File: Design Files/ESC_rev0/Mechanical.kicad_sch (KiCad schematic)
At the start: 8 parts

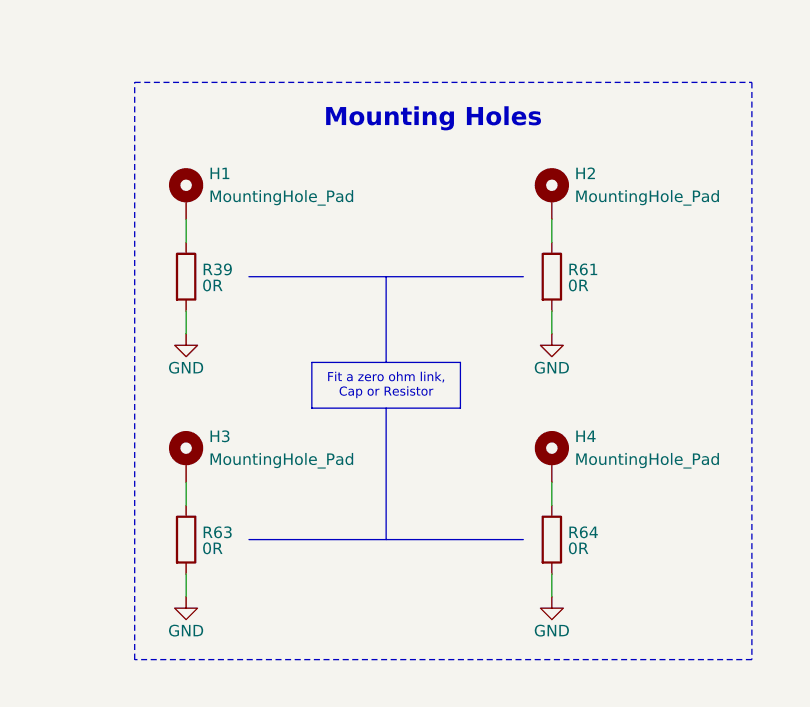
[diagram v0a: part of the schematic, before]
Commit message: UPDATE 12
started schematics revision: edit and added info and circuits to some pages and assigned some footprints for components
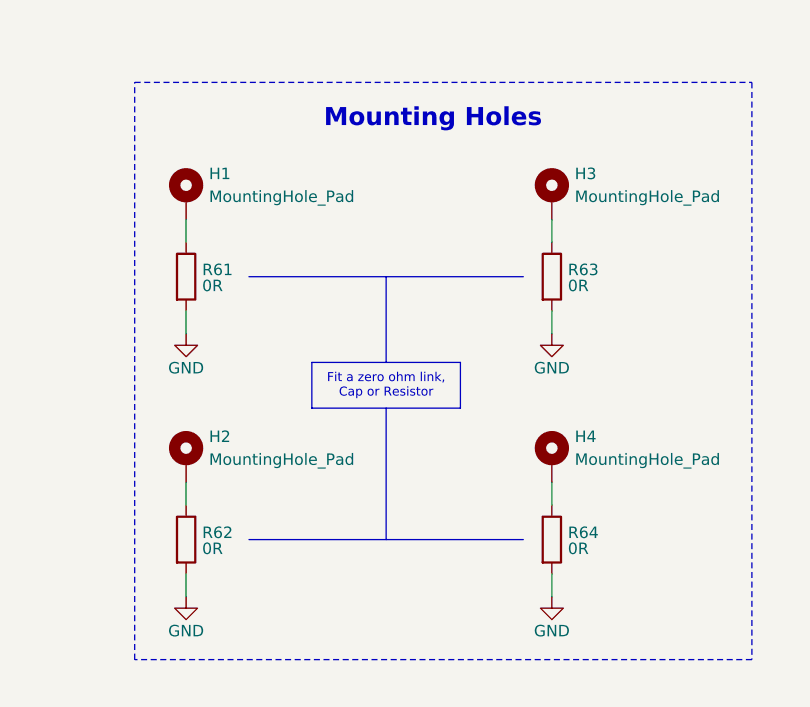
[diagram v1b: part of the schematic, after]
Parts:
- renumbered H3 to H2, H2 to H3, R39 to R61, R63 to R62, R61 to R63
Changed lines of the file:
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@@
 		(on_board yes)
 		(dnp no)
-		(property "Reference" "#PWR088"
+		(property "Reference" "#PWR087"
 			(at 120.65 125.73 0)
 			(effects
@@
 			(project "ESC_rev0"
 				(path "/7906e740-34c4-4b06-b70f-1daa08872946/abbcb70d-9199-4d8d-b98d-11d4883ec6c1"
-					(reference "#PWR088")
+					(reference "#PWR087")
 					(unit 1)
 				)
@@
 		(dnp no)
 		(fields_autoplaced yes)
-		(property "Reference" "H2"
+		(property "Reference" "H3"
 			(at 163.83 72.3899 0)
 			(effects
@@
 			(project "ESC_rev0"
 				(path "/7906e740-34c4-4b06-b70f-1daa08872946/abbcb70d-9199-4d8d-b98d-11d4883ec6c1"
-					(reference "H2")
+					(reference "H3")
 					(unit 1)
 				)
@@
 		(on_board yes)
 		(dnp no)
-		(property "Reference" "H3"
+		(property "Reference" "H2"
 			(at 123.19 101.5999 0)
 			(effects
@@
 			(project "ESC_rev0"
 				(path "/7906e740-34c4-4b06-b70f-1daa08872946/abbcb70d-9199-4d8d-b98d-11d4883ec6c1"
-					(reference "H3")
+					(reference "H2")
 					(unit 1)
 				)
@@
 		(on_board yes)
 		(dnp no)
-		(property "Reference" "#PWR050"
+		(property "Reference" "#PWR086"
 			(at 120.65 96.52 0)
 			(effects
@@
 			(project ""
 				(path "/7906e740-34c4-4b06-b70f-1daa08872946/abbcb70d-9199-4d8d-b98d-11d4883ec6c1"
-					(reference "#PWR050")
+					(reference "#PWR086")
 					(unit 1)
 				)
@@
 		(on_board yes)
 		(dnp no)
-		(property "Reference" "R61"
+		(property "Reference" "R63"
 			(at 163.068 83.0581 0)
 			(effects
@@
 			(project "ESC_rev0"
 				(path "/7906e740-34c4-4b06-b70f-1daa08872946/abbcb70d-9199-4d8d-b98d-11d4883ec6c1"
-					(reference "R61")
+					(reference "R63")
 					(unit 1)
 				)
@@
 		(on_board yes)
 		(dnp no)
-		(property "Reference" "R63"
+		(property "Reference" "R62"
 			(at 122.428 112.2681 0)
 			(effects
@@
 			(project "ESC_rev0"
 				(path "/7906e740-34c4-4b06-b70f-1daa08872946/abbcb70d-9199-4d8d-b98d-11d4883ec6c1"
-					(reference "R63")
+					(reference "R62")
 					(unit 1)
 				)
@@
 		(on_board yes)
 		(dnp no)
-		(property "Reference" "#PWR051"
+		(property "Reference" "#PWR088"
 			(at 161.29 96.52 0)
 			(effects
@@
 			(project "ESC_rev0"
 				(path "/7906e740-34c4-4b06-b70f-1daa08872946/abbcb70d-9199-4d8d-b98d-11d4883ec6c1"
-					(reference "#PWR051")
+					(reference "#PWR088")
 					(unit 1)
 				)
@@
 		(on_board yes)
 		(dnp no)
-		(property "Reference" "R39"
+		(property "Reference" "R61"
 			(at 122.428 83.0581 0)
 			(effects
@@
 			(project ""
 				(path "/7906e740-34c4-4b06-b70f-1daa08872946/abbcb70d-9199-4d8d-b98d-11d4883ec6c1"
-					(reference "R39")
-					(unit 1)
-				)
+					(reference "R61")
+					(unit 1)
+				)

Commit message: update 13
assigned all footprints (provisionally) and imported them - errors and warning occurred, must be corrected in the future
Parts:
- H1, H2, H3, H4: footprint (none) -> MountingHole:MountingHole_3.2mm_M3
- R61, R62, R63, R64: footprint (none) -> Resistor_SMD:R_0603_1608Metric
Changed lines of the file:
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@@
 			)
 		)
-		(property "Footprint" ""
+		(property "Footprint" "MountingHole:MountingHole_3.2mm_M3"
 			(at 161.29 74.93 0)
 			(effects
@@
 			)
 		)
-		(property "Footprint" ""
+		(property "Footprint" "MountingHole:MountingHole_3.2mm_M3"
 			(at 120.65 104.14 0)
 			(effects
@@
 			)
 		)
-		(property "Footprint" ""
+		(property "Footprint" "Resistor_SMD:R_0603_1608Metric"
 			(at 159.512 83.82 90)
 			(effects
@@
 			)
 		)
-		(property "Footprint" ""
+		(property "Footprint" "Resistor_SMD:R_0603_1608Metric"
 			(at 118.872 113.03 90)
 			(effects
@@
 			)
 		)
-		(property "Footprint" ""
+		(property "Footprint" "MountingHole:MountingHole_3.2mm_M3"
 			(at 120.65 74.93 0)
 			(effects
@@
 			)
 		)
-		(property "Footprint" ""
+		(property "Footprint" "Resistor_SMD:R_0603_1608Metric"
 			(at 159.512 113.03 90)
 			(effects
@@
 			)
 		)
-		(property "Footprint" ""
+		(property "Footprint" "MountingHole:MountingHole_3.2mm_M3"
 			(at 161.29 104.14 0)
 			(effects
@@
 			)
 		)
-		(property "Footprint" ""
+		(property "Footprint" "Resistor_SMD:R_0603_1608Metric"
 			(at 118.872 83.82 90)
 			(effects

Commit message: update 15
Simple connectors replaced by smd connectors (downloaded). Connectors were placed in edges of the board.
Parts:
- H1, H2, H3, H4: footprint MountingHole:MountingHole_3.2mm_M3 -> MountingHole:MountingHole_3.2mm_M3_Pad_Via
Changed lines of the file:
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@@
 			)
 		)
-		(property "Footprint" "MountingHole:MountingHole_3.2mm_M3"
+		(property "Footprint" "MountingHole:MountingHole_3.2mm_M3_Pad_Via"
 			(at 161.29 74.93 0)
 			(effects
@@
 			)
 		)
-		(property "Footprint" "MountingHole:MountingHole_3.2mm_M3"
+		(property "Footprint" "MountingHole:MountingHole_3.2mm_M3_Pad_Via"
 			(at 120.65 104.14 0)
 			(effects
@@
 			)
 		)
-		(property "Footprint" "MountingHole:MountingHole_3.2mm_M3"
+		(property "Footprint" "MountingHole:MountingHole_3.2mm_M3_Pad_Via"
 			(at 120.65 74.93 0)
 			(effects
@@
 			)
 		)
-		(property "Footprint" "MountingHole:MountingHole_3.2mm_M3"
+		(property "Footprint" "MountingHole:MountingHole_3.2mm_M3_Pad_Via"
 			(at 161.29 104.14 0)
 			(effects

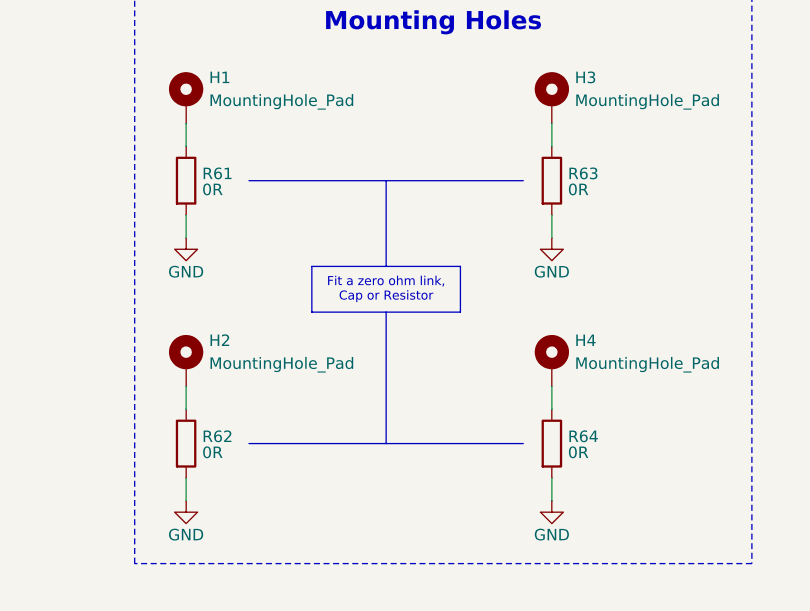
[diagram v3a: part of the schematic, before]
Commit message: update 16
All components placed on board. Some components modifications and addition were made: added 3D models, changed some symbols and footprints positions and some component types.
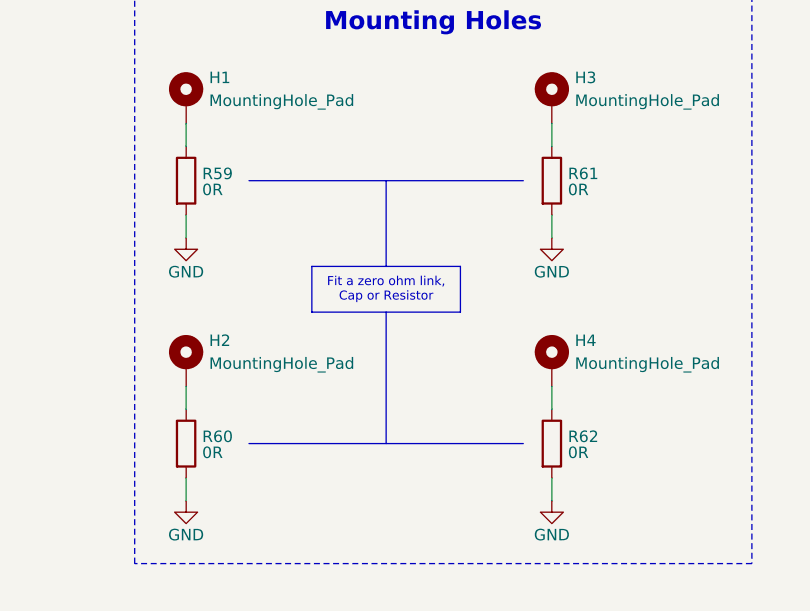
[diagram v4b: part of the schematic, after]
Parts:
- renumbered R61 to R59, R62 to R60, R63 to R61, R64 to R62
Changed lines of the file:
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@@
 		(on_board yes)
 		(dnp no)
-		(property "Reference" "#PWR087"
+		(property "Reference" "#PWR083"
 			(at 120.65 125.73 0)
 			(effects
@@
 			(project "ESC_rev0"
 				(path "/7906e740-34c4-4b06-b70f-1daa08872946/abbcb70d-9199-4d8d-b98d-11d4883ec6c1"
-					(reference "#PWR087")
+					(reference "#PWR083")
 					(unit 1)
 				)
@@
 		(on_board yes)
 		(dnp no)
-		(property "Reference" "#PWR086"
+		(property "Reference" "#PWR082"
 			(at 120.65 96.52 0)
 			(effects
@@
 			(project ""
 				(path "/7906e740-34c4-4b06-b70f-1daa08872946/abbcb70d-9199-4d8d-b98d-11d4883ec6c1"
-					(reference "#PWR086")
+					(reference "#PWR082")
 					(unit 1)
 				)
@@
 		(on_board yes)
 		(dnp no)
-		(property "Reference" "R63"
+		(property "Reference" "R61"
 			(at 163.068 83.0581 0)
 			(effects
@@
 			(project "ESC_rev0"
 				(path "/7906e740-34c4-4b06-b70f-1daa08872946/abbcb70d-9199-4d8d-b98d-11d4883ec6c1"
-					(reference "R63")
+					(reference "R61")
 					(unit 1)
 				)
@@
 		(on_board yes)
 		(dnp no)
-		(property "Reference" "R62"
+		(property "Reference" "R60"
 			(at 122.428 112.2681 0)
 			(effects
@@
 			(project "ESC_rev0"
 				(path "/7906e740-34c4-4b06-b70f-1daa08872946/abbcb70d-9199-4d8d-b98d-11d4883ec6c1"
-					(reference "R62")
+					(reference "R60")
 					(unit 1)
 				)
@@
 		(on_board yes)
 		(dnp no)
-		(property "Reference" "R64"
+		(property "Reference" "R62"
 			(at 163.068 112.2681 0)
 			(effects
@@
 			(project "ESC_rev0"
 				(path "/7906e740-34c4-4b06-b70f-1daa08872946/abbcb70d-9199-4d8d-b98d-11d4883ec6c1"
-					(reference "R64")
+					(reference "R62")
 					(unit 1)
 				)
@@
 		(on_board yes)
 		(dnp no)
-		(property "Reference" "#PWR088"
+		(property "Reference" "#PWR084"
 			(at 161.29 96.52 0)
 			(effects
@@
 			(project "ESC_rev0"
 				(path "/7906e740-34c4-4b06-b70f-1daa08872946/abbcb70d-9199-4d8d-b98d-11d4883ec6c1"
-					(reference "#PWR088")
+					(reference "#PWR084")
 					(unit 1)
 				)
@@
 		(on_board yes)
 		(dnp no)
-		(property "Reference" "#PWR089"
+		(property "Reference" "#PWR085"
 			(at 161.29 125.73 0)
 			(effects
@@
 			(project "ESC_rev0"
 				(path "/7906e740-34c4-4b06-b70f-1daa08872946/abbcb70d-9199-4d8d-b98d-11d4883ec6c1"
-					(reference "#PWR089")
+					(reference "#PWR085")
 					(unit 1)
 				)
@@
 		(on_board yes)
 		(dnp no)
-		(property "Reference" "R61"
+		(property "Reference" "R59"
 			(at 122.428 83.0581 0)
 			(effects
@@
 			(project ""
 				(path "/7906e740-34c4-4b06-b70f-1daa08872946/abbcb70d-9199-4d8d-b98d-11d4883ec6c1"
-					(reference "R61")
-					(unit 1)
-				)
+					(reference "R59")
+					(unit 1)
+				)

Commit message: update 22
Board complete - not perfect for production, it is just a demo.  Generated gerber files through extensions, prepared some layout infos, updated the schematics with images. Note: due to a power outage, the last update had conflicts and the push was forced.
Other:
- note added: "Layer 1 - Front"
- note added: "Layer 2 - Inner GND"
- note added: "Layer 3 - Inner GND"
- note added: "Layer 4 - Back"
- note added: "Modifications from VESC 4.11"
- note removed: "Modification from VESC 4.11:"
- note removed: "PCB"
- moved on the sheet: H1, H2, H3, H4, R59, R60, R61, R62
